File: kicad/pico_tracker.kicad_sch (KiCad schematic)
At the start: 28 parts, among them J1 MIDI_OUT, J10 DclassAMP, J11 MASTER_VOLUME, J2 MIDI_IN, J3 MIDI_IN_A_B_VCC, J4 MIDI_IN_A_B_DATA, J5 MIDI_OUT_A_B_VCC, J6 MIDI_OUT_A_B_DATA, J7 DISPLAY, J8 SDCARD, J9 KILL_SWITCH, SW1 LEFT, SW2 DOWN, SW3 RIGHT, SW4 UP, SW5 RT, SW6 B, SW7 A, SW8 LT, SW9 PLAY, U1 Pico, U2 6N138, U3 PCM5102_Module

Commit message: Add files via upload
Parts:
- removed J11: MASTER_VOLUME, Connector_PinHeader_2.54mm:PinHeader_2x03_P2.54mm_Vertical_SMD, symbol Connector:Conn_01x06_Female
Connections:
- net LOUT is gone; now on net L_AMP: U3.15 (LOUT)
- net ROUT is gone; now on net R_AMP: U3.13 (ROUT)

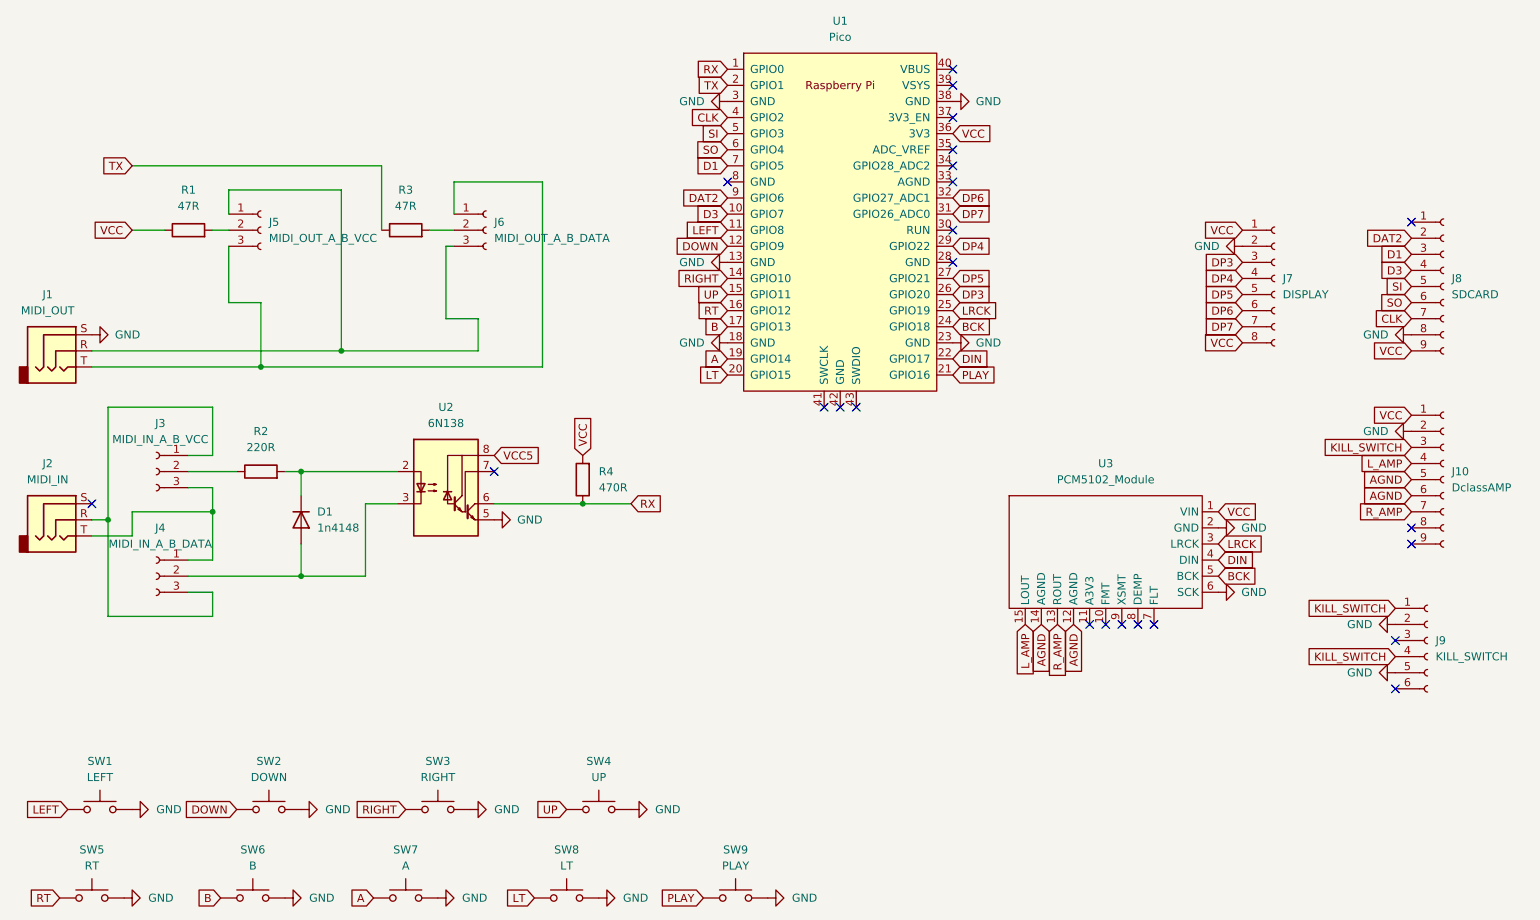
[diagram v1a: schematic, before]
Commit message: fix: 6N138 VCC connexion and RX/TX pins flip
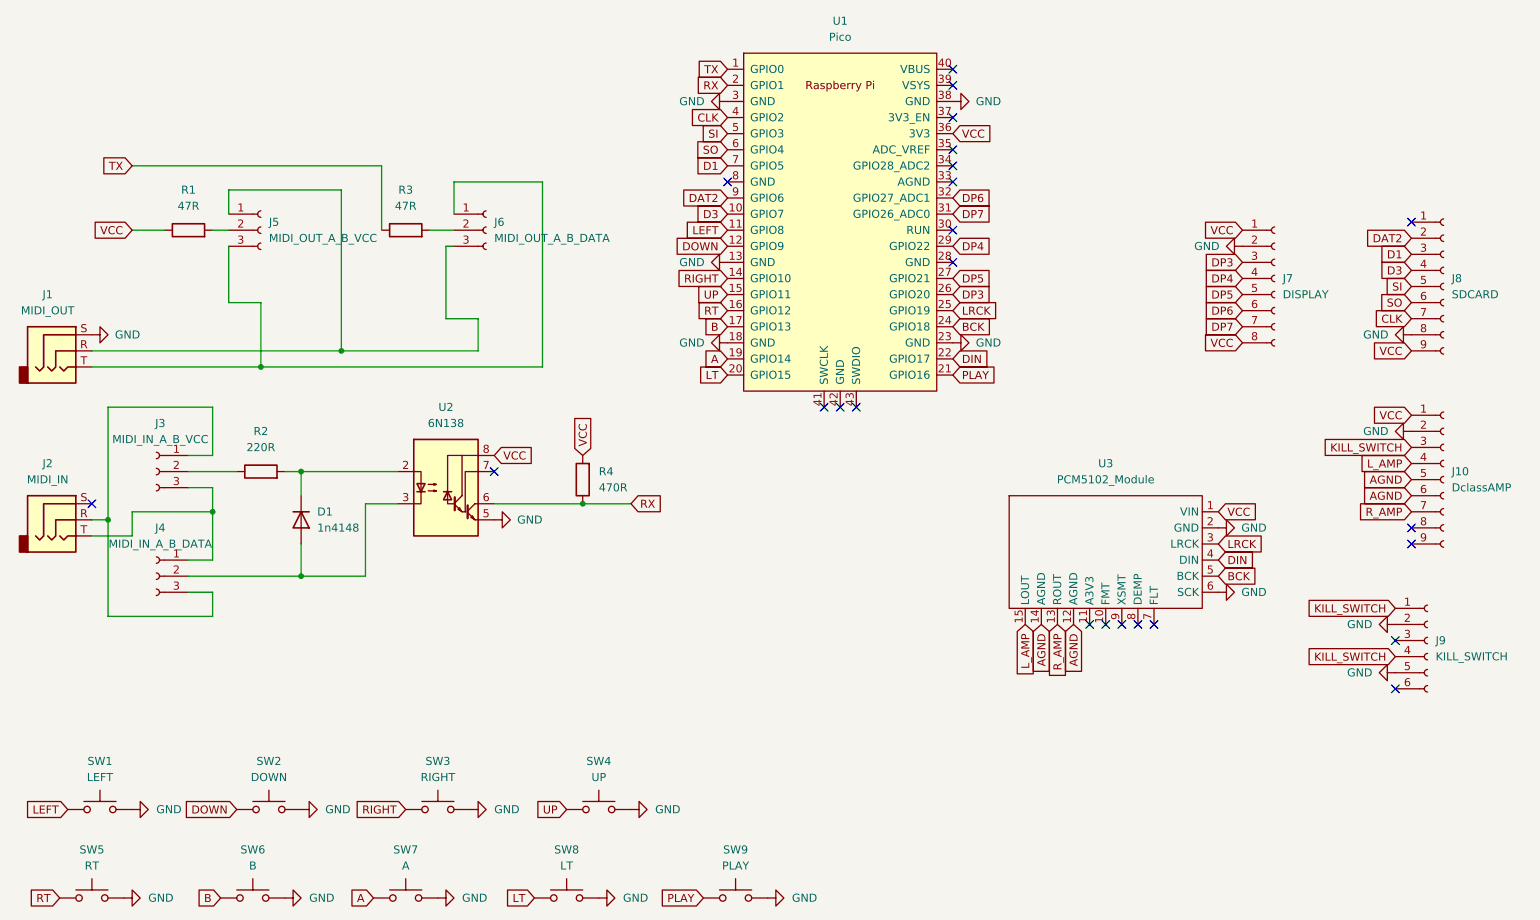
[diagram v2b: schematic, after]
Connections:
- net VCC5 is gone; now on net VCC: U2.8 (VCC)
- net RX: now also U1.2 (GPIO1); no longer U1.1 (GPIO0)
- net TX: now also U1.1 (GPIO0); no longer U1.2 (GPIO1)

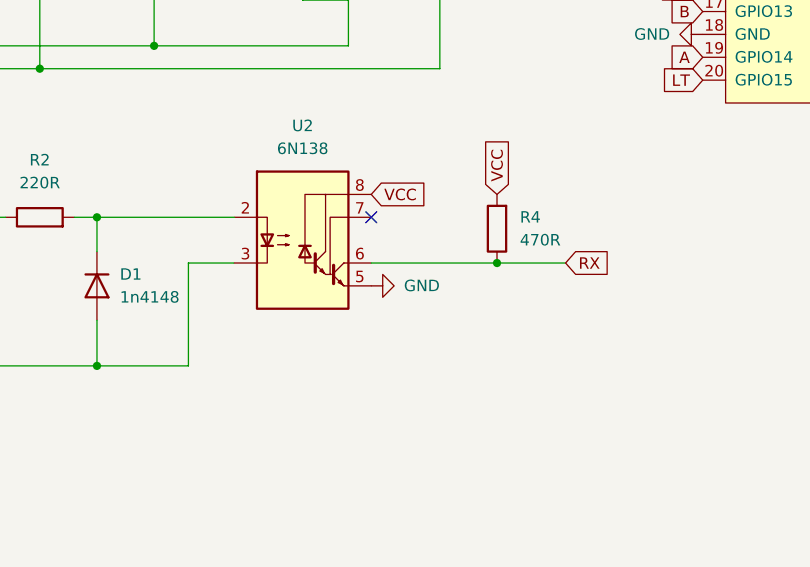
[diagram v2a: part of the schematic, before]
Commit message: fix: add 10k resistor to pin 7
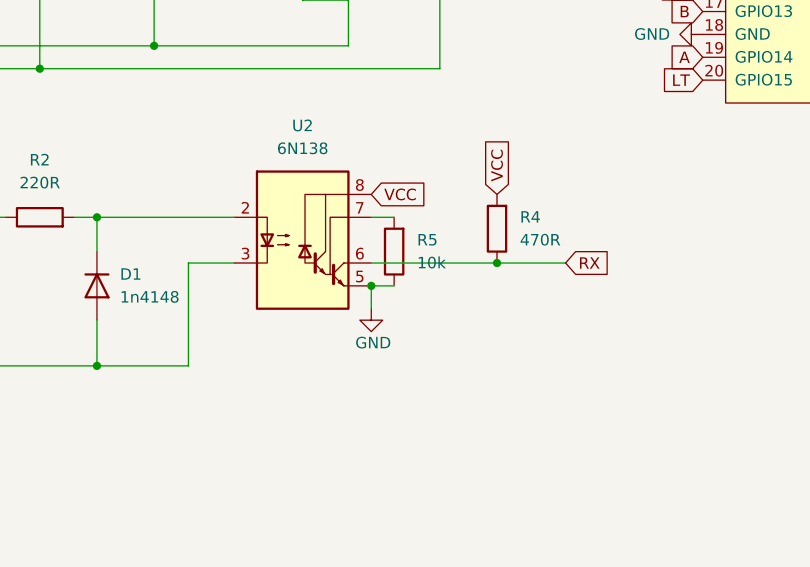
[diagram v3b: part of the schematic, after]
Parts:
- added R5: 10k, Resistor_SMD:R_0603_1608Metric, symbol Device:R
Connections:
- net GND: now also R5.1
- net at U2.7 (VO1): now also R5.2
- no-connect marks 24 -> 23
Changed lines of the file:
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@@
 	)
 	(junction
+		(at 100.33 124.46)
+		(diameter 0)
+		(color 0 0 0 0)
+	)
+	(junction
 		(at 39.37 124.46)
 		(diameter 0)
@@
 	)
 	(no_connect
-		(at 100.33 116.84)
-	)
-	(no_connect
 		(at 172.72 55.88)
 	)
@@
 	(wire
 		(pts
+			(xy 100.33 127) (xy 100.33 124.46)
+		)
+		(stroke
+			(width 0)
+			(type default)
+		)
+	)
+	(wire
+		(pts
 			(xy 39.37 139.7) (xy 39.37 124.46)
 		)
@@
 	(wire
 		(pts
+			(xy 102.87 116.84) (xy 100.33 116.84)
+		)
+		(stroke
+			(width 0)
+			(type default)
+		)
+	)
+	(wire
+		(pts
 			(xy 82.55 78.74) (xy 82.55 68.58)
 		)
@@
 	(wire
 		(pts
+			(xy 102.87 124.46) (xy 100.33 124.46)
+		)
+		(stroke
+			(width 0)
+			(type default)
+		)
+	)
+	(wire
+		(pts
 			(xy 43.18 78.74) (xy 48.26 78.74)
 		)
@@
 	(symbol
 		(lib_id "power:GND")
-		(at 100.33 124.46 90)
+		(at 100.33 127 0)
 		(unit 1)
 		(exclude_from_sim no)
@@
 		(dnp no)
 		(property "Reference" "#PWR08"
-			(at 106.68 124.46 0)
+			(at 100.33 133.35 0)
 			(effects
 				(font
@@
 		)
 		(property "Value" "GND"
-			(at 107.95 124.46 90)
+			(at 98.552 130.81 0)
 			(effects
 				(font
@@
 		)
 		(property "Footprint" ""
-			(at 100.33 124.46 0)
+			(at 100.33 127 0)
 			(effects
 				(font
@@
 		)
 		(property "Datasheet" ""
-			(at 100.33 124.46 0)
+			(at 100.33 127 0)
 			(effects
 				(font
@@
 		)
 		(property "Description" ""
-			(at 100.33 124.46 0)
+			(at 100.33 127 0)
 			(effects
 				(font
@@
 					(unit 1)
 				)
+			)
+		)
+	)
+	(symbol
+		(lib_id "Device:R")
+		(at 102.87 120.65 180)
+		(unit 1)
+		(exclude_from_sim no)
+		(in_bom yes)
+		(on_board yes)
+		(dnp no)
+		(fields_autoplaced yes)
+		(property "Reference" "R5"
+			(at 105.41 119.3799 0)
+			(effects
+				(font
+					(size 1.27 1.27)
+				)
+				(justify right)
+			)
+		)
+		(property "Value" "10k"
+			(at 105.41 121.9199 0)
+			(effects
+				(font
+					(size 1.27 1.27)
+				)
+				(justify right)
+			)
+		)
+		(property "Footprint" "Resistor_SMD:R_0603_1608Metric"
+			(at 104.648 120.65 90)
+			(effects
+				(font
+					(size 1.27 1.27)
+				)
+				(hide yes)
+			)
+		)
+		(property "Datasheet" "~"
+			(at 102.87 120.65 0)
+			(effects
+				(font
+					(size 1.27 1.27)
+				)
+				(hide yes)
+			)
+		)
+		(property "Description" ""
+			(at 102.87 120.65 0)
+			(effects
+				(font
+					(size 1.27 1.27)
+				)
+			)
+		)
+		(pin "1"
+		)
+		(pin "2"
+		)
+		(instances
+			(project "pico_tracker"
+				(path "/01db86bd-26c2-4e39-9ead-bae04a2202f6"
+					(reference "R5")
+					(unit 1)
+				)
